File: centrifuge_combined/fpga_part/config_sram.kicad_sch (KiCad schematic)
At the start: 6 parts, among them U1 XC7A100T-FTG256, U2 S25FL127SABMFV10, U3 CY7C1370KV33

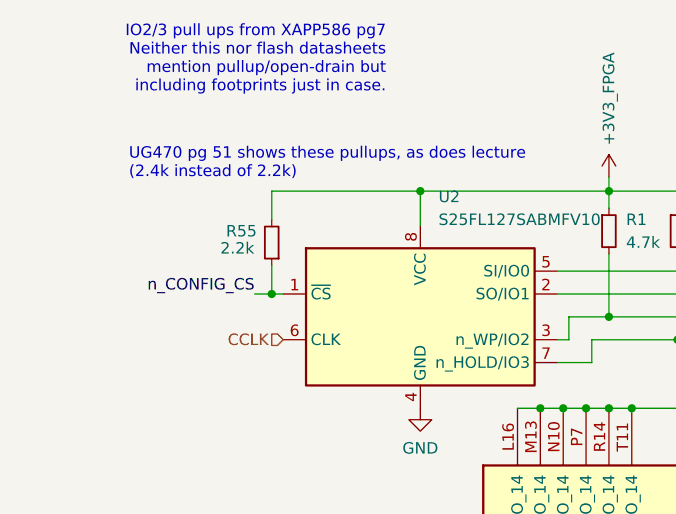
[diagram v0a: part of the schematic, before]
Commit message: change resistor values to have to 2k2, and also make I2C hopefully work
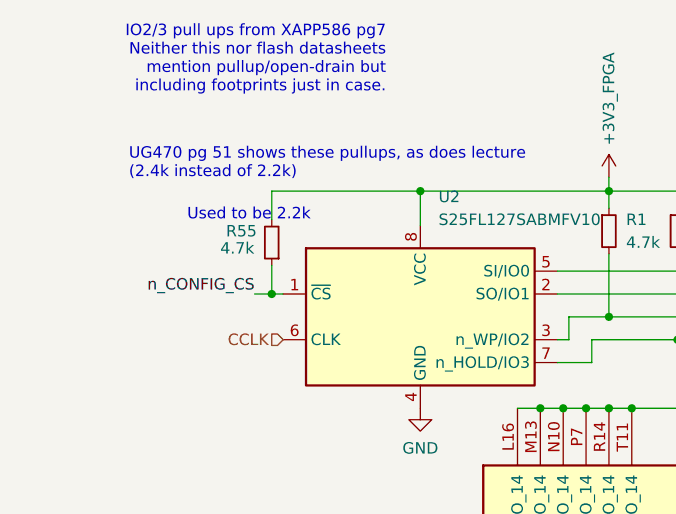
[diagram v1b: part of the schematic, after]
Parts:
- R55: value 2.2k -> 4.7k
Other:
- note added: "Used to be 2.2k"
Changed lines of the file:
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@@
+    (effects (font (size 1.27 1.27)) (justify left bottom))
+  )
+  (text "Used to be 2.2k" (at 22.352 23.114 0)
     (effects (font (size 1.27 1.27)) (justify left bottom))
   )
@@
       (effects (font (size 1.27 1.27)) (justify right))
     )
-    (property "Value" "2.2k" (id 1) (at 26.035 26.035 0)
+    (property "Value" "4.7k" (id 1) (at 26.035 26.035 0)
       (effects (font (size 1.27 1.27)) (justify right))
     )
